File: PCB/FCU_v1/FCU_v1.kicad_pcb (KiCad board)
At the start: 4 copper layers, 57.6 x 60.8 mm, 105 parts, among them IC2 BMM350, IC3 TPS7A2018PDBVR, IC4 ESP32-C3-MINI-1-N4X, J1 Conn_01x04_Pin, J10 Conn_01x04_Pin, J11 USB_C_Receptacle_USB2.0_16P, J3 Conn_01x05_Pin, J5 Conn_01x04_Pin, J6 Conn_01x04_Pin, J7 Conn_01x04_Pin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

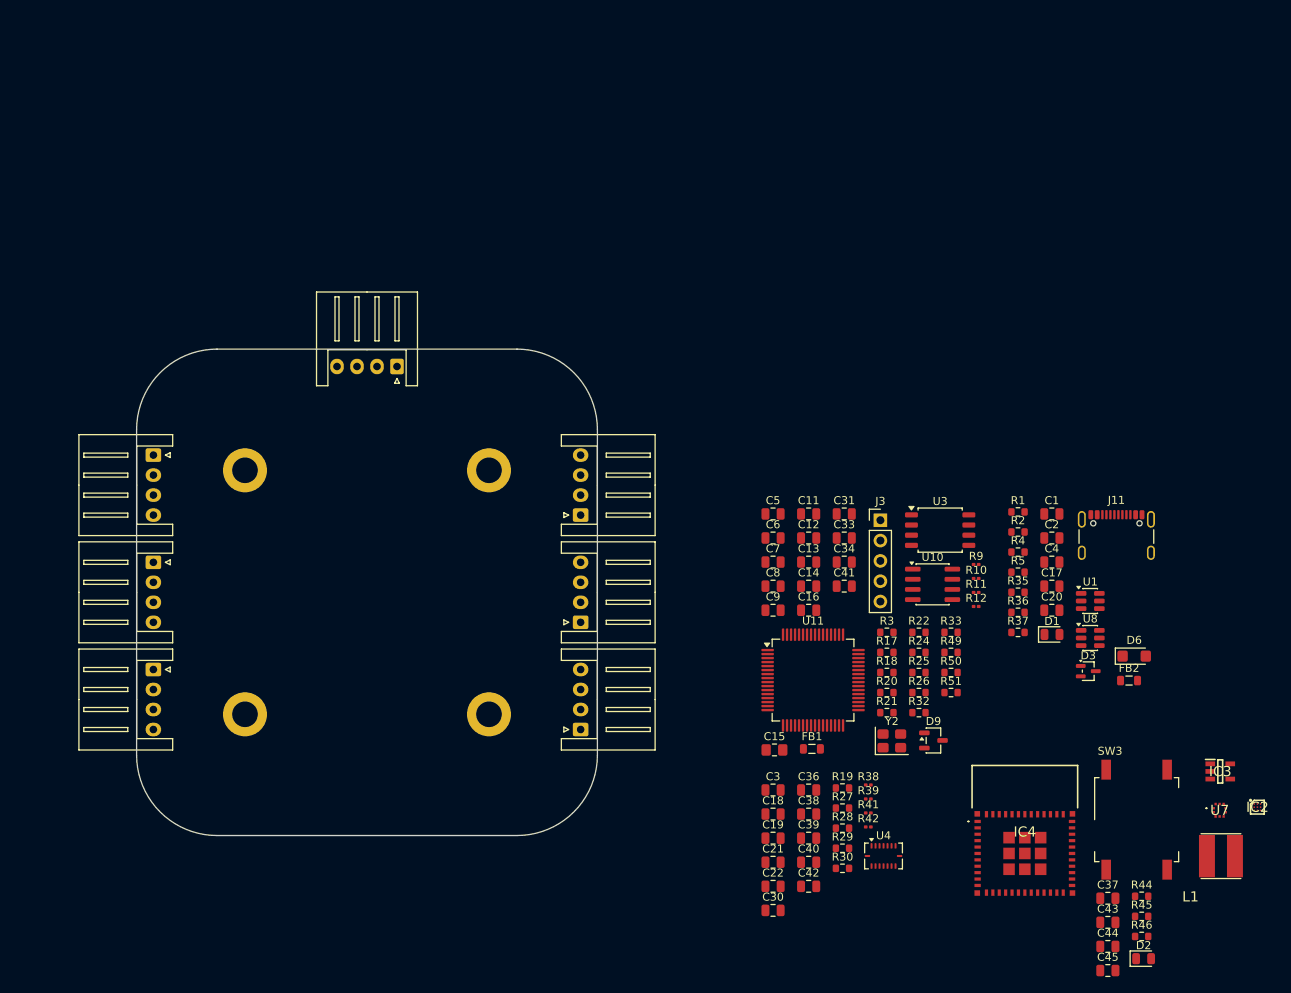
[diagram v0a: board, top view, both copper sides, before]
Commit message: Components change and layout update
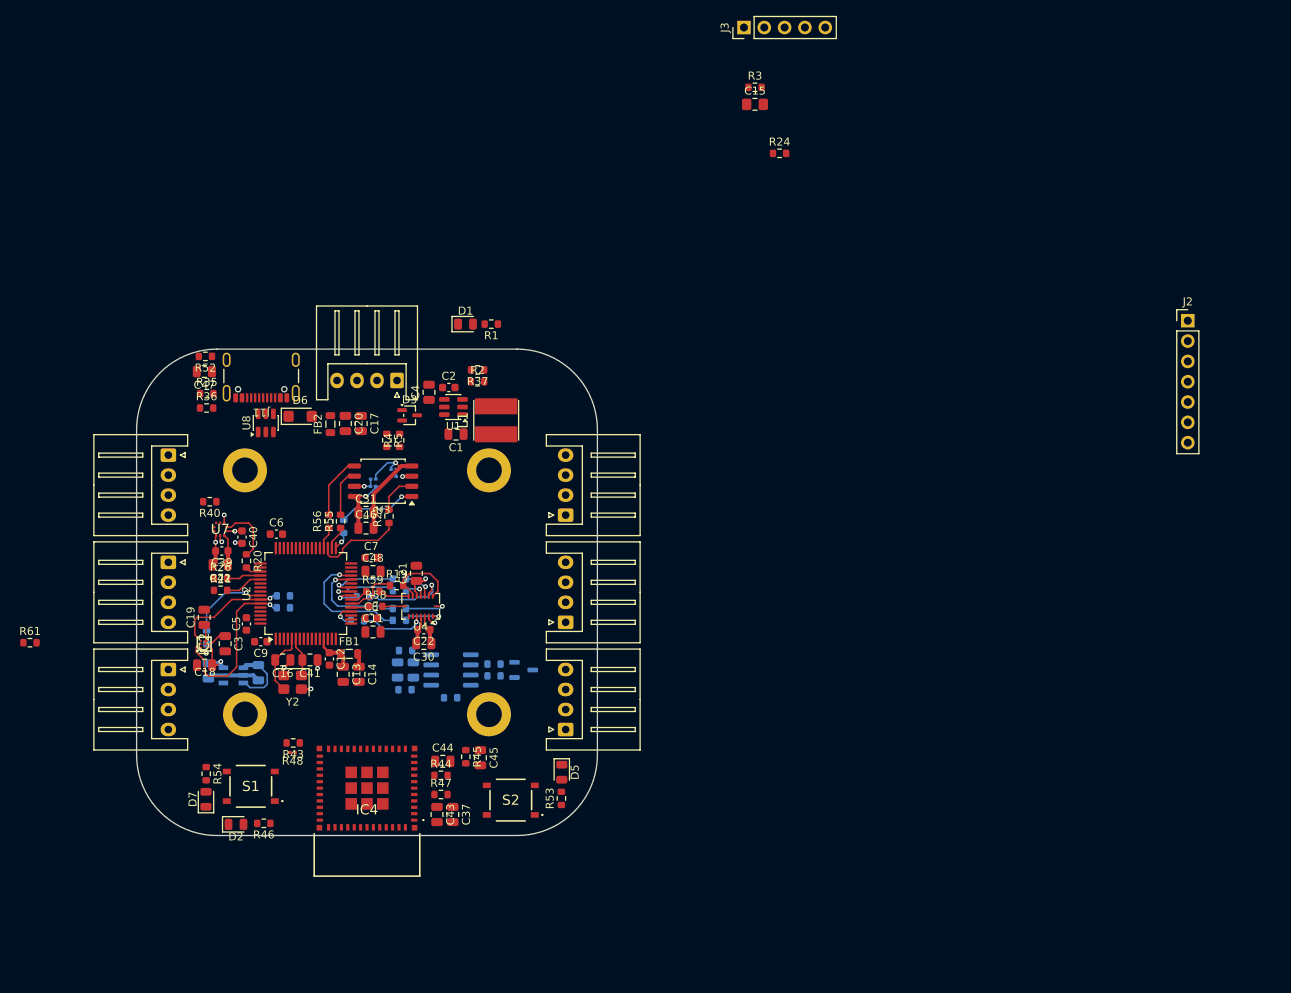
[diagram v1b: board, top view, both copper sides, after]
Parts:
- removed R38, R39, R41, R42: DNP, Resistor_SMD:R_0201_0603Metric
- removed SW3: SW_MEC_5G, Button_Switch_SMD:SW_MEC_5GSH9
- removed U11: STM32G473RETx, Package_QFP:LQFP-64_10x10mm_P0.5mm
- added C46: 10u, Capacitor_SMD:C_0805_2012Metric, F.Cu at (128.7, 78.7)
- added C47: 22u, Capacitor_SMD:C_0805_2012Metric, F.Cu at (108.5, 59.1)
- added C48: 4u7, Capacitor_SMD:C_0805_2012Metric, F.Cu at (129.6, 84.1)
- added D5: LED, LED_SMD:LED_0805_2012Metric, F.Cu at (153.2, 109.2)
- added D7: LED, LED_SMD:LED_0805_2012Metric, F.Cu at (108.7, 112.6)
- added J2: Conn_01x07_Pin, Connector_PinHeader_2.54mm:PinHeader_1x07_P2.54mm_Vertical, F.Cu at (231.4, 52.8)
- added R40: 33R, Resistor_SMD:R_0603_1608Metric, F.Cu at (109.2, 75.4)
- added R43: 10k, Resistor_SMD:R_0603_1608Metric, F.Cu at (119.6, 105.5)
- added R47: 10k, Resistor_SMD:R_0603_1608Metric, F.Cu at (138.1, 112.0)
- added R48: DNP, Resistor_SMD:R_0201_0603Metric, F.Cu at (119.5, 106.8)
- added R52: 5k1, Resistor_SMD:R_0603_1608Metric, F.Cu at (108.6, 57.2)
- added R53: 4k7, Resistor_SMD:R_0603_1608Metric, F.Cu at (153.1, 112.5)
- added R54: 4k7, Resistor_SMD:R_0603_1608Metric, F.Cu at (108.7, 109.4)
- added R55: 33R, Resistor_SMD:R_0603_1608Metric, F.Cu at (125.5, 77.8)
- added R56: 33R, Resistor_SMD:R_0603_1608Metric, F.Cu at (124.0, 77.8)
- added R57: 33R, Resistor_SMD:R_0603_1608Metric, B.Cu at (125.9, 78.5)
- added R58: 33R, Resistor_SMD:R_0603_1608Metric, F.Cu at (129.9, 88.5)
- added R59: 33R, Resistor_SMD:R_0603_1608Metric, F.Cu at (129.6, 86.6)
- added R6: 33R, Resistor_SMD:R_0603_1608Metric, B.Cu at (108.8, 92.3)
- added R60: 33R, Resistor_SMD:R_0603_1608Metric, B.Cu at (127.6, 90.3)
- added R61: 33R, Resistor_SMD:R_0603_1608Metric, F.Cu at (86.7, 93.0)
- added S1: PTS526SM15SMTR2_LFS, SamacSys_Parts:PTS526SM15SMTR2LFS, F.Cu at (114.3, 111.0)
- added S2: PTS526SM15SMTR2_LFS, SamacSys_Parts:PTS526SM15SMTR2LFS, F.Cu at (146.8, 112.7)
- added U2: STM32F412RETx, Package_QFP:LQFP-64_10x10mm_P0.5mm, F.Cu at (121.2, 86.9)
- C1: value 22u/10V -> 22u/6.3V
- C12, C2, C22, C39, C40, C5, C6, C7, C8, C9: footprint Capacitor_SMD:C_0805_2012Metric -> Capacitor_SMD:C_0603_1608Metric
- C17: value 22u -> 22u/10V
- C20: value 100n -> 100n/10V
- C33, C34, C36, C38, D9, IC3, R10, R11, R12, R17, R18, R25, R27, R28, R29, R30, R32, R33, R49, R50, R51, R9, U10: moved to B.Cu
- R46: value 2k -> 4k7
- moved IC2 133.2 mm to (108.5, 93.2), turned to 90 degrees
- moved U7 129.8 mm to (110.5, 78.8), turned to 180 degrees
- moved IC3 123.9 mm to (112.1, 97.1), turned to 180 degrees
- moved D2 114.7 mm to (112.5, 115.7)
- moved R46 110.6 mm to (115.9, 115.6), turned to 180 degrees
- moved J11 109.1 mm to (115.6, 58.7), turned to 180 degrees
- moved D6 108.5 mm to (120.5, 64.7)
- moved U8 106.5 mm to (116.2, 65.5), turned to 90 degrees
- moved L1 105.7 mm to (145.0, 65.2), turned to -90 degrees
- moved FB2 104.9 mm to (124.2, 65.7), turned to 90 degrees
- moved R36 104.6 mm to (108.8, 63.7)
- moved R35 104.4 mm to (108.8, 61.9)
- moved C20 91.3 mm to (126.1, 65.6), turned to -90 degrees
- moved D3 90.7 mm to (134.2, 64.6)
- moved R44 88.9 mm to (138.1, 109.6)
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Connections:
- net Net-(IC2-CRST) renamed /IMU/CRST_MAG
- net Net-(IC2-VDD) renamed /IMU/VDD_BAR
- net Net-(IC4-EN) renamed ESP_EN
- net Net-(U4-INT1) renamed /IMU/ACCE1_INT
- net Net-(U4-INT2) renamed /IMU/ACCE2_INT
- net Net-(U4-INT3) renamed /IMU/GYRO1_INT
- net Net-(U4-INT4) renamed /IMU/GYRO2_INT
- net Net-(U4-SDO1) renamed /IMU/SPI1_MISO_ACCE
- D3 pad 1: +VBUS -> +5V
- D3 pad 2: +5V -> +VBUS
- IC2 pad A1: MAG_INT -> /IMU/MAG_INT
- IC2 pad A3: I2C_SCK -> I2C_SCL
- IC2 pad B2: Net-(IC2-ADSEL) -> GND
- IC4 pad 22: unconnected-(IC4-IO8-Pad22) -> ESP_GPIO8
- IC4 pad 23: unconnected-(IC4-IO9-Pad23) -> ESP_GPIO9
- IC4 pad 5: unconnected-(IC4-IO2-Pad5) -> ESP_GPIO2
- J11 pad S1: GND -> Net-(J11-SHIELD)
- R19 pad 1: SPI_MISO -> SPI1_MISO
- R20 pad 1: SPI_SCK -> SPI3_SCK
- R20 pad 2: SPI_SCK -> /MCU/SPI3_SCK_STM
- R21 pad 1: SPI_MOSI -> SPI3_MOSI
- R21 pad 2: SPI_MOSI -> /MCU/SPI3_MOSI_STM
- R22 pad 1: SPI_MISO -> SPI2_MISO
- R24 pad 1: CSB_ACCEL -> CS_BARO
- R24 pad 2: /MCU/CSB_ACCE -> /MCU/CS_BARO_STM
- R25 pad 1: CSB_GYRO -> CS_ACCE
- R25 pad 2: /MCU/CSB_GYR -> /MCU/CSB_ACCE_STM
- R26 pad 1: CS_MEMO -> /IMU/SPI3_MISO_BAR
- R26 pad 2: /MCU/CS_MEM -> SPI3_MISO
- R27 pad 1: INT1_ACCEL -> INT_ACCE1
- R28 pad 1: INT2_ACCEL -> INT_ACCE2
- R29 pad 1: INT1_GYRO -> INT_GYRO1
- R30 pad 1: INT2_GYRO -> INT_GYRO2
- U3 pad 5: SPI_MOSI -> SPI2_MOSI
- U3 pad 6: SPI_SCK -> SPI2_SCK
- U4 pad 14: CSB_ACCEL -> CS_ACCE
- U4 pad 5: CSB_GYRO -> CS_GYRO
- U4 pad 8: SPI_SCK -> SPI1_SCK
- U4 pad 9: SPI_MOSI -> SPI1_MOSI
- U7 pad 2: I2C_SCK -> SPI3_SCK
- U7 pad 4: I2C_SDA -> SPI3_MOSI
- U7 pad 5: Net-(U7-SDO) -> /IMU/SPI3_MISO_BAR
- U7 pad 6: STM_VDD -> CS_BARO
- U7 pad 7: BAR_INT -> /IMU/BAR_INT
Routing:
- net GND: track 0.00 -> 39.0 mm, vias 0 -> 9
- net STM_VDD: track 0.00 -> 34.9 mm, vias 0 -> 3
- net I2C_SDA: track 0.00 -> 21.6 mm, vias 0 -> 1
- net INT_ACCE2: track 0.00 -> 15.9 mm, vias 0 -> 1
- net I2C_SCL: track 0.00 -> 14.5 mm, vias 0 -> 1
- net INT_ACCE1: track 0.00 -> 12.8 mm, vias 0 -> 1
- net CS_ACCE: track 0.00 -> 11.1 mm, vias 0 -> 1
- net SPI2_MISO: track 0.00 -> 11.0 mm
- net INT_MAG: track 0.00 -> 10.2 mm, vias 0 -> 1
- net /IMU/SPI1_MISO_ACCE: track 0.00 -> 9.84 mm
- net CS_MEMO: track 0.00 -> 9.73 mm, vias 0 -> 1
- net INT_GYRO1: track 0.00 -> 8.76 mm, vias 0 -> 1
- net INT_GYRO2: track 0.00 -> 8.68 mm, vias 0 -> 1
- net CS_GYRO: track 0.00 -> 8.21 mm, vias 0 -> 1
- net OSC_IN: track 0.00 -> 7.98 mm
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
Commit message: Layout update
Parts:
- removed IC2: BMM350, SamacSys_Parts:BGA9C40P3X3_128X128X54
- removed J2: Conn_01x07_Pin, Connector_PinHeader_2.54mm:PinHeader_1x07_P2.54mm_Vertical
- removed L1: 744042001, SamacSys_Parts:WE-TPC_4818_482892
- removed R49, R50: 22Ω, Resistor_SMD:R_0603_1608Metric
- removed S1: PTS526SM15SMTR2_LFS, SamacSys_Parts:PTS526SM15SMTR2LFS
- added IC1: BMM350, SamacSys_Parts:BGA9C40P3X3_128X128X54, F.Cu at (108.5, 90.3)
- added J12: Conn_01x02_Pin, Connector_PinHeader_2.54mm:PinHeader_1x02_P2.54mm_Vertical, F.Cu at (108.8, 64.5)
- added J13: Conn_01x02_Pin, Connector_PinHeader_2.54mm:PinHeader_1x02_P2.54mm_Vertical, F.Cu at (111.2, 64.5)
- added J14: Conn_01x02_Pin, Connector_PinHeader_2.54mm:PinHeader_1x02_P2.54mm_Vertical, F.Cu at (107.2, 111.0)
- added J15: Conn_01x02_Pin, Connector_PinHeader_2.54mm:PinHeader_1x02_P2.54mm_Vertical, F.Cu at (113.0, 113.5)
- added J16: Conn_01x02_Pin, Connector_PinHeader_2.54mm:PinHeader_1x02_P2.54mm_Vertical, F.Cu at (110.0, 111.0)
- added J17: Conn_01x01_Pin, Connector_PinHeader_2.54mm:PinHeader_1x01_P2.54mm_Vertical, F.Cu at (149.2, 105.0)
- added L4: 744042001, SamacSys_Parts:WE-TPC_4818_482892, F.Cu at (144.9, 65.0)
- added R38: 4k7, Resistor_SMD:R_0603_1608Metric, F.Cu at (128.8, 101.8)
- added R39: DNP, Resistor_SMD:R_0201_0603Metric, B.Cu at (119.5, 85.2)
- added R41: 10k, Resistor_SMD:R_0603_1608Metric, F.Cu at (106.0, 65.0)
- added R42: DNP, Resistor_SMD:R_0201_0603Metric, F.Cu at (106.0, 63.0)
- added S3: PTS526SM15SMTR2_LFS, SamacSys_Parts:PTS526SM15SMTR2LFS, F.Cu at (117.8, 111.8)
- C15, C47, R24, R3, R35, R36, R40, R52, R61: moved to B.Cu
- C33, C34, D9, R10, R11, R12, R17, R18, R32, R51, R57, R9, U10: moved to F.Cu
- IC3: value TPS7A2018PDBVR -> ESP32-C3-MINI-1-N4X; footprint SamacSys_Parts:SOT95P280X145-5N -> SamacSys_Parts:ESP32C3MINI1N4X; moved to F.Cu
- IC4: value ESP32-C3-MINI-1-N4X -> TPS7A2018PDBVR; footprint SamacSys_Parts:ESP32C3MINI1N4X -> SamacSys_Parts:SOT95P280X145-5N; moved to B.Cu
- J3: value Conn_01x05_Pin -> Conn_01x02_Pin; footprint Connector_PinHeader_2.54mm:PinHeader_1x05_P2.54mm_Vertical -> Connector_PinHeader_2.54mm:PinHeader_1x02_P2.54mm_Vertical
- U7: value BMP581 -> USBLC6-2SC6; footprint SamacSys_Parts:BMP581 -> Package_TO_SOT_SMD:SOT-23-6
- U8: value USBLC6-2SC6 -> BMP581; footprint Package_TO_SOT_SMD:SOT-23-6 -> SamacSys_Parts:BMP581
- moved J3 87.7 mm to (108.8, 72.5), turned to 180 degrees
- moved C15 87.2 mm to (121.5, 92.7)
- moved R3 86.5 mm to (118.5, 87.0)
- moved R24 84.1 mm to (113.5, 82.9)
- moved R61 39.1 mm to (125.8, 94.8), turned to -90 degrees
- moved D2 25.4 mm to (133.5, 101.5), turned to 90 degrees
- moved IC4 24.9 mm to (111.8, 95.8)
- moved IC3 22.9 mm to (128.8, 112.7)
- moved R46 21.5 mm to (131.8, 101.0), turned to 90 degrees
- moved D1 14.4 mm to (151.8, 63.0), turned to 180 degrees
- moved R1 14.3 mm to (151.8, 65.5), turned to 0 degrees
- moved U7 14.3 mm to (115.7, 65.5), turned to 90 degrees
- moved D7 13.3 mm to (119.0, 104.2), turned to 180 degrees
- moved R33 12.7 mm to (121.7, 89.8)
- moved U8 12.0 mm to (111.3, 76.5), turned to 180 degrees
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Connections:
- D9 pad 1: CAN_H -> CAN+
- D9 pad 2: CAN_L -> CAN-
- IC3 pad 1: STM_VDD -> GND
- IC3 pad 5: /IMU/VDD_BAR -> ESP_GPIO2
- IC4 pad 1: GND -> STM_VDD
- IC4 pad 5: ESP_GPIO2 -> /IMU/VDD_BAR
- J10 pad 3: CAN_L -> CAN-
- J10 pad 4: CAN_H -> CAN+
- J3 pad 2: SWDIO -> GND
- J5 pad 3: CAN_L -> CAN-
- J5 pad 4: CAN_H -> CAN+
- J6 pad 3: CAN_L -> CAN-
- J6 pad 4: CAN_H -> CAN+
- J7 pad 3: CAN_L -> CAN-
- J7 pad 4: CAN_H -> CAN+
- J8 pad 3: CAN_L -> CAN-
- J8 pad 4: CAN_H -> CAN+
- J9 pad 3: CAN_L -> CAN-
- J9 pad 4: CAN_H -> CAN+
- R32 pad 1: CAN_TX -> CAN_RX
- R32 pad 2: Net-(U10-D) -> Net-(U10-R)
- R33 pad 1: CAN_RX -> /MCU/CAN_TX_STM
- R33 pad 2: Net-(U10-R) -> CAN_TX
- R46 pad 1: Net-(IC4-IO5) -> Net-(IC3-IO5)
- R51 pad 1: Net-(U10-CANL) -> CAN-
- R51 pad 2: Net-(U10-CANH) -> CAN+
- U1 pad 3: Net-(U1-SW) -> /SW_TPS
- U10 pad 1: Net-(U10-D) -> CAN_TX
- U10 pad 6: Net-(U10-CANL) -> CAN-
- U10 pad 7: Net-(U10-CANH) -> CAN+
- U2 pad 10: BAT_CURR -> BAT_VOL
- U2 pad 17: USART2_TX -> USART2_RX
- U2 pad 62: CAN_TX -> /MCU/CAN_TX_STM
- U2 pad 9: BAT_VOL -> BAT_CURR
- U7 pad 1: STM_VDD -> USB_D+
- U7 pad 2: SPI3_SCK -> GND
- U7 pad 3: GND -> USB_D-
- U7 pad 4: SPI3_MOSI -> /D-
- U7 pad 5: /IMU/SPI3_MISO_BAR -> /USB_VBUS
- U7 pad 6: CS_BARO -> /D+
- U8 pad 1: USB_D+ -> STM_VDD
- U8 pad 2: GND -> SPI3_SCK
- U8 pad 3: USB_D- -> GND
- U8 pad 4: /D- -> SPI3_MOSI
- U8 pad 5: /USB_VBUS -> /IMU/SPI3_MISO_BAR
- U8 pad 6: /D+ -> CS_BARO
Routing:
- net STM_VDD: track 34.9 -> 294.9 mm, vias 3 -> 21
- net CAN-: track 0.00 -> 158.0 mm, vias 0 -> 1
- net CAN+: track 0.00 -> 156.5 mm, vias 0 -> 1
- net BAT_VOL: track 0.00 -> 35.7 mm, vias 0 -> 1
- net NRST: track 0.00 -> 35.3 mm, vias 0 -> 2
- net BAT_CURR: track 0.00 -> 34.0 mm, vias 0 -> 1
- net GND: track 39.0 -> 69.1 mm, vias 9 -> 601
- net SWO: track 0.00 -> 28.8 mm, vias 0 -> 1
- net CAN_RX: track 0.00 -> 26.2 mm, vias 0 -> 2
- net ESP_GPIO9: track 0.00 -> 26.1 mm
- net ESP_GPIO8: track 0.00 -> 24.5 mm
- net SWCLK: track 0.00 -> 24.3 mm, vias 0 -> 1
- net SWDIO: track 0.00 -> 22.2 mm, vias 0 -> 1
- net ESP_EN: track 0.00 -> 20.3 mm, vias 0 -> 2
- net CAN_TX: track 0.00 -> 18.6 mm, vias 0 -> 1
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- added copper zone on F.Cu, net +5V
- added copper zone on In2.Cu, net +5V
- added copper zone on F.Cu, net +5V_FCU
- added copper zone on F.Cu, net /SW_TPS
- added copper zone on B.Cu, net GND
- added copper zone on F.Cu, net GND
- added copper zone on F.Cu, net STM_VDD
- added copper zone on In2.Cu, net STM_VDD

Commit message: Layout update
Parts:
- R42: footprint Resistor_SMD:R_0201_0603Metric -> Resistor_SMD:R_0402_1005Metric
- moved R6 2.02 mm to (110.0, 91.0), turned to 180 degrees
- moved R42 0.25 mm to (106.0, 62.8)
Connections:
- J12 pad 1: NRST -> SWO
- J12 pad 2: SWDIO -> SWCLK
- J13 pad 1: SWCLK -> NRST
- J13 pad 2: SWO -> SWDIO
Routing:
- net GND: track 69.1 -> 83.4 mm, vias 601 -> 158
- net STM_VDD: track 294.9 -> 306.6 mm, vias 21 -> 22
- net NRST: track 35.3 -> 42.1 mm
- net /USB_VBUS: track 9.61 -> 15.7 mm, vias 0 -> 2
- net SWO: track 28.8 -> 33.3 mm
- net SWCLK: track 24.3 -> 28.0 mm
- net CAN-: track 158.0 -> 161.7 mm
- net CAN+: track 156.5 -> 160.2 mm
- net Net-(D2-A): track 0.00 -> 1.91 mm
- net Net-(R41-Pad2): track 0.00 -> 1.64 mm
- net SWDIO: track 22.2 -> 23.2 mm
- net /IMU/VDD_BAR: track 10.0 -> 9.51 mm
- net (no net): vias 147 -> 576

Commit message: Layout cleanup + PCB view
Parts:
- moved R22 0.68 mm to (131.1, 76.3)
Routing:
- net GND: vias 158 -> 156
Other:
- board text added: "FCU v1 02/26"
- board text added: "X"
- board text added: "Y"

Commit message: Layout update
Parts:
- added IC2: TCAN3414DR, SamacSys_Parts:SOIC127P600X175-8N, F.Cu at (3.75, 2.77)
- C16, C41: value 10p -> 6p8; footprint Capacitor_SMD:C_0805_2012Metric -> Capacitor_SMD:C_0603_1608Metric
- C34, C43: footprint Capacitor_SMD:C_0805_2012Metric -> Capacitor_SMD:C_0603_1608Metric
- FB1: value 120R at 100 MHz -> FCM1608KF-601T03; footprint Inductor_SMD:L_0805_2012Metric -> Inductor_SMD:L_0603_1608Metric
- R10, R11, R12, R39, R48, R9: footprint Resistor_SMD:R_0201_0603Metric -> Resistor_SMD:R_0402_1005Metric
- Y2: value 16MHz -> 24MHz
- moved R41 2.40 mm to (103.6, 64.9)
- moved R42 0.78 mm to (105.3, 62.4)
- moved J15 0.47 mm to (112.5, 113.5)
- moved C41 0.41 mm to (120.7, 95.5)
- moved J3 0.38 mm to (108.8, 72.1)
- moved C33 0.38 mm to (134.2, 96.3)
- moved C37 0.38 mm to (139.0, 113.3)
- moved R10 0.30 mm to (135.2, 70.7)
- moved C16 0.29 mm to (117.7, 95.5)
- moved R48 0.21 mm to (121.8, 102.0)
- moved C43 0.20 mm to (137.2, 113.3)
- moved C34 0.20 mm to (136.0, 96.3)
- moved C6 0.15 mm to (117.1, 79.5)
- moved R11 0.15 mm to (128.6, 68.5)
- moved FB1 0.12 mm to (126.3, 94.7)
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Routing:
- net GND: track 83.4 -> 87.9 mm, vias 156 -> 122
- net STM_VDD: track 306.6 -> 308.2 mm
- net Net-(R41-Pad2): track 1.64 -> 2.51 mm
- net NRST: track 42.1 -> 42.9 mm
- net +5V_FCU: track 8.99 -> 9.57 mm
- net (no net): vias 576 -> 0
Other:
- board text added: "3.3V"
- board text added: "5V"
- board text added: "BATT_CURR"
- board text added: "BATT_VOL"
- board text added: "CANH"
- board text added: "CANL"
- board text added: "CLK"
- board text added: "DBG"
- board text added: "DIO"
- board text added: "EN"
- board text added: "FCU v1 03/26"
- board text added: "GN"
- board text added: "GND"
- board text added: "IO8"
- board text added: "IO9"
- board text added: "PWR"
- board text added: "RST"
- board text added: "SWO"
- board text removed: "FCU v1 02/26"
